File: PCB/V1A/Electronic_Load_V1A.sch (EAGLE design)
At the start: 64 parts, among them J1 +, J2 -, J3 +, J4 -, Q1 IXTK102N65X2, Q2 IXTK102N65X2, Q3 IRF540, Q4 IRF540, Q5 IRF540, Q6 IRF540, U1 LTC1865-MSOP, U2 LTC1865-MSOP, U3 AD420, U4 AD420

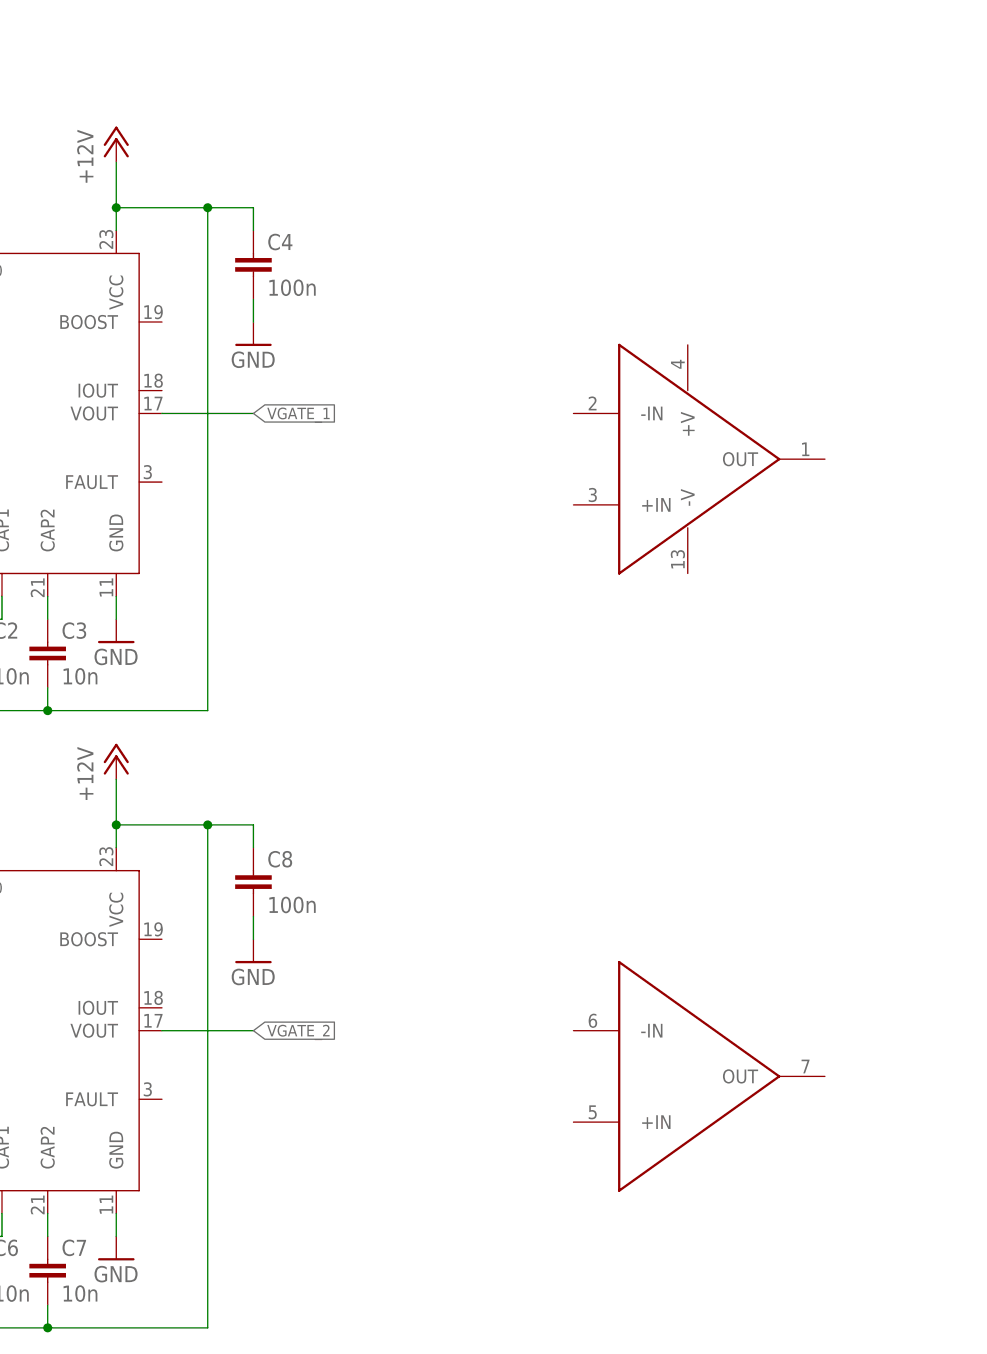
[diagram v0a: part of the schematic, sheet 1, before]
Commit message: Added buffer amplifiers
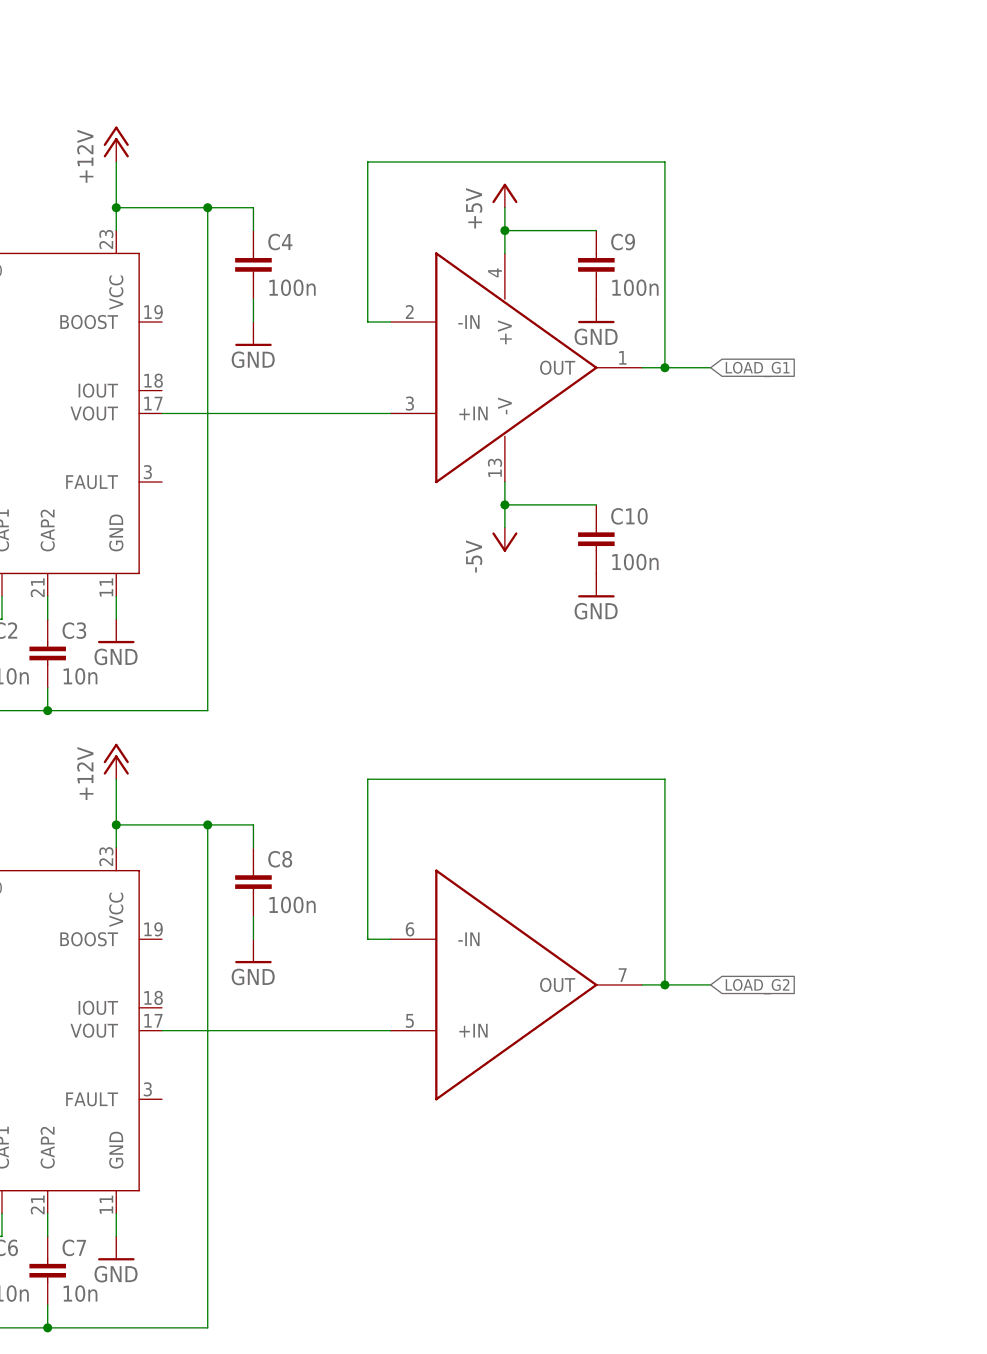
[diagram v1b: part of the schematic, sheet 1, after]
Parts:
- added C10, C9: 100n, rcl:C-EUC0805
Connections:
- net +5V: now also C9.1, U$2G1.+V
- net -5V: now also C10.1, U$2G1.-V
- net GND: now also C10.2, C9.2
- net LOAD_G1: now also U$2G1.-IN, U$2G1.OUT
- net LOAD_G2: now also U$2G2.-IN, U$2G2.OUT
- net VGATE_1: now also U$2G1.+IN
- net VGATE_2: now also U$2G2.+IN
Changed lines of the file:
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@@
 <?xml version="1.0" encoding="utf-8"?>
 <!DOCTYPE eagle SYSTEM "eagle.dtd">
-<eagle version="9.0.0">
+<eagle version="9.0.1">
 <drawing>
 <settings>
@@
 <part name="GND17" library="supply1" library_urn="urn:adsk.eagle:library:371" deviceset="GND" device=""/>
 <part name="U$2" library="SparkFun-Retired" deviceset="LT1014" device=""/>
+<part name="P+12" library="supply1" library_urn="urn:adsk.eagle:library:371" deviceset="+5V" device=""/>
+<part name="P-3" library="supply1" library_urn="urn:adsk.eagle:library:371" deviceset="-5V" device=""/>
+<part name="C9" library="rcl" library_urn="urn:adsk.eagle:library:334" deviceset="C-EU" device="C0805" package3d_urn="urn:adsk.eagle:package:23617/2" value="100n"/>
+<part name="C10" library="rcl" library_urn="urn:adsk.eagle:library:334" deviceset="C-EU" device="C0805" package3d_urn="urn:adsk.eagle:package:23617/2" value="100n"/>
+<part name="GND18" library="supply1" library_urn="urn:adsk.eagle:library:371" deviceset="GND" device=""/>
+<part name="GND19" library="supply1" library_urn="urn:adsk.eagle:library:371" deviceset="GND" device=""/>
 </parts>
 <sheets>
@@
 <instance part="C8" gate="G$1" x="104.14" y="147.32"/>
 <instance part="GND17" gate="1" x="104.14" y="137.16"/>
-<instance part="U$2" gate="G1" x="149.86" y="193.04"/>
-<instance part="U$2" gate="G2" x="149.86" y="124.46"/>
+<instance part="U$2" gate="G1" x="129.54" y="203.2"/>
+<instance part="U$2" gate="G2" x="129.54" y="134.62"/>
 <instance part="U$2" gate="G3" x="-88.9" y="231.14"/>
 <instance part="U$2" gate="G4" x="-91.44" y="180.34"/>
+<instance part="P+12" gate="1" x="132.08" y="223.52"/>
+<instance part="P-3" gate="1" x="132.08" y="182.88"/>
+<instance part="C9" gate="G$1" x="142.24" y="215.9"/>
+<instance part="C10" gate="G$1" x="142.24" y="185.42"/>
+<instance part="GND18" gate="1" x="142.24" y="208.28"/>
+<instance part="GND19" gate="1" x="142.24" y="177.8"/>
 </instances>
 <busses>
@@
 <wire x1="104.14" y1="142.24" x2="104.14" y2="139.7" width="0.1524" layer="91"/>
 </segment>
+<segment>
+<pinref part="C9" gate="G$1" pin="2"/>
+<pinref part="GND18" gate="1" pin="GND"/>
+</segment>
+<segment>
+<pinref part="C10" gate="G$1" pin="2"/>
+<pinref part="GND19" gate="1" pin="GND"/>
+</segment>
 </net>
 <net name="N$1" class="0">
@@
 <label x="198.12" y="114.3" size="1.27" layer="95" font="vector" ratio="12" rot="R180" xref="yes"/>
 <pinref part="R1" gate="G$1" pin="1"/>
+</segment>
+<segment>
+<pinref part="U$2" gate="G1" pin="-IN"/>
+<wire x1="119.38" y1="208.28" x2="116.84" y2="208.28" width="0.1524" layer="91"/>
+<wire x1="116.84" y1="208.28" x2="116.84" y2="226.06" width="0.1524" layer="91"/>
+<wire x1="116.84" y1="226.06" x2="149.86" y2="226.06" width="0.1524" layer="91"/>
+<wire x1="149.86" y1="226.06" x2="149.86" y2="203.2" width="0.1524" layer="91"/>
+<pinref part="U$2" gate="G1" pin="OUT"/>
+<wire x1="149.86" y1="203.2" x2="147.32" y2="203.2" width="0.1524" layer="91"/>
+<wire x1="149.86" y1="203.2" x2="154.94" y2="203.2" width="0.1524" layer="91"/>
+<junction x="149.86" y="203.2"/>
+<label x="154.94" y="203.2" size="1.27" layer="95" font="vector" ratio="12" xref="yes"/>
 </segment>
 </net>
@@
 <wire x1="261.62" y1="114.3" x2="256.54" y2="114.3" width="0.1524" layer="91"/>
 <label x="256.54" y="114.3" size="1.27" layer="95" font="vector" ratio="12" rot="R180" xref="yes"/>
+</segment>
+<segment>
+<pinref part="U$2" gate="G2" pin="-IN"/>
+<wire x1="119.38" y1="139.7" x2="116.84" y2="139.7" width="0.1524" layer="91"/>
+<wire x1="116.84" y1="139.7" x2="116.84" y2="157.48" width="0.1524" layer="91"/>
+<wire x1="116.84" y1="157.48" x2="149.86" y2="157.48" width="0.1524" layer="91"/>
+<wire x1="149.86" y1="157.48" x2="149.86" y2="134.62" width="0.1524" layer="91"/>
+<pinref part="U$2" gate="G2" pin="OUT"/>
+<wire x1="149.86" y1="134.62" x2="147.32" y2="134.62" width="0.1524" layer="91"/>
+<wire x1="149.86" y1="134.62" x2="154.94" y2="134.62" width="0.1524" layer="91"/>
+<junction x="149.86" y="134.62"/>
+<label x="154.94" y="134.62" size="1.27" layer="95" font="vector" ratio="12" xref="yes"/>
 </segment>
 </net>
@@
 <pinref part="P+11" gate="1" pin="+5V"/>
 </segment>
+<segment>
+<pinref part="U$2" gate="G1" pin="+V"/>
+<pinref part="P+12" gate="1" pin="+5V"/>
+<wire x1="132.08" y1="220.98" x2="132.08" y2="218.44" width="0.1524" layer="91"/>
+<pinref part="C9" gate="G$1" pin="1"/>
+<wire x1="132.08" y1="218.44" x2="132.08" y2="215.9" width="0.1524" layer="91"/>
+<wire x1="132.08" y1="218.44" x2="142.24" y2="218.44" width="0.1524" layer="91"/>
+<junction x="132.08" y="218.44"/>
+</segment>
 </net>
 <net name="VGATE_1" class="0">
 <segment>
 <pinref part="U3" gate="G$1" pin="VOUT"/>
-<wire x1="93.98" y1="198.12" x2="104.14" y2="198.12" width="0.1524" layer="91"/>
-<label x="104.14" y="198.12" size="1.27" layer="95" font="vector" ratio="12" xref="yes"/>
+<pinref part="U$2" gate="G1" pin="+IN"/>
+<wire x1="119.38" y1="198.12" x2="93.98" y2="198.12" width="0.1524" layer="91"/>
 </segment>
 </net>
@@
 <segment>
 <pinref part="U4" gate="G$1" pin="VOUT"/>
-<wire x1="93.98" y1="129.54" x2="104.14" y2="129.54" width="0.1524" layer="91"/>
-<label x="104.14" y="129.54" size="1.27" layer="95" font="vector" ratio="12" xref="yes"/>
-</segment>
-</net>
+<pinref part="U$2" gate="G2" pin="+IN"/>
+<wire x1="119.38" y1="129.54" x2="93.98" y2="129.54" width="0.1524" layer="91"/>
+</segment>
+</net>
+<net name="-5V" class="0">
+<segment>
+<pinref part="U$2" gate="G1" pin="-V"/>
+<pinref part="P-3" gate="1" pin="-5V"/>
+<wire x1="132.08" y1="185.42" x2="132.08" y2="187.96" width="0.1524" layer="91"/>
+<pinref part="C10" gate="G$1" pin="1"/>
+<wire x1="132.08" y1="187.96" x2="132.08" y2="190.5" width="0.1524" layer="91"/>
+<wire x1="132.08" y1="187.96" x2="142.24" y2="187.96" width="0.1524" layer="91"/>
+<junction x="132.08" y="187.96"/>
+</segment>
+</net>

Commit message: Updated DAC buffer amps & datasheets
Changed the positive supply of DAC buffer op amps from +5V to +12V, added input offset trimming and set their gain to 2 (1.98). This was done in order to achieve maximum current at low voltages by increasing the maximum gate voltage, and to cailbrate the op amps.
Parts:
- removed C1, C10, C4, C5, C8, C9: 100n, rcl:C-EUC0805
- removed C2, C3, C6, C7: 10n, rcl:C-EUC0805
- removed J1, J3: +, SparkFun-Connectors:BANANA_CONN
- removed J2, J4: -, SparkFun-Connectors:BANANA_CONN
- removed Q1, Q2: IXTK102N65X2, transistors:IXTK102N65X2
- removed Q3, Q4, Q5, Q6: IRF540, transistor-fet:IRF540
- removed R1, R2, R3, R4, R5, R8, R9: 100R, rcl:R-EU_M5923
- removed R10, R6: 2R, rcl:R-EU_M5923
- removed R11, R7: 0R002, rcl:R-EU_M5923
- removed S1: (no value), switch:320-938
- removed U$2: LT1014, SparkFun-Retired:LT1014
- removed U3, U4: AD420, adc_dac:AD420
- added C101, C102, C107, C108, C109, C110: 100n, rcl:C-EUC0805
- added C103, C104, C105, C106: 10n, rcl:C-EUC0805
- added J101, J103: +, SparkFun-Connectors:BANANA_CONN
- added J102, J104: -, SparkFun-Connectors:BANANA_CONN
- added Q101, Q102, Q103, Q105, Q106, Q107: SIRC10DP, transistors:SIRC10DP
- added Q104, Q108: IXTK102N65X2, transistors:IXTK102N65X2
- added R101, R102: 20k, rcl:R-TRIMM4G/J
- added R103, R104: 200k, rcl:R-EU_M5923
- added R105, R106, R111, R112, R113, R114, R115, R118, R119, R120, R121: 100R, rcl:R-EU_M5923
- added R107, R108, R109, R110: 5k, rcl:R-EU_M5923
- added R116, R122: 2R, rcl:R-EU_M5923
- added R117, R123: 0R002, rcl:R-EU_M5923
- added S101: (no value), switch:320-938
- added U101, U102: AD420, adc_dac:AD420
- added U103: LT1014, SparkFun-Retired:LT1014
- renumbered R12 to R201, R13 to R209, R14 to R202, R15 to R205, R16 to R206, R17 to R210, R18 to R213, R19 to R203, R20 to R211, R21 to R204, R22 to R207, R23 to R208, R24 to R212, R25 to R214, R26 to R215, R27 to R223, R28 to R216, R29 to R219, R30 to R220, R31 to R224, R32 to R227, R33 to R217, R34 to R225, R35 to R218, R36 to R221, R37 to R222, R38 to R226, R39 to R228, U$1 to U201, U1 to U202, U2 to U203
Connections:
- new net N$28: R107.2, R109.1, U103G1.-IN
- new net N$29: R108.2, R110.1, U103G2.-IN
- new net N$30: Q101.G, R112.2
- new net N$31: Q105.G, R118.2
- new net N$32: R103.2, R105.2, R107.1
- new net N$33: R101.S, R103.1
- new net N$34: R102.S, R104.1
- new net N$35: R104.2, R106.2, R108.1
- net +12V: now also C103.2, C104.2, C105.2, C106.2, C107.1, C108.1, C109.1, U101.VCC, U102.VCC, U103G1.+V; no longer C2.2, C3.2, C4.1, C6.2, C7.2, C8.1, U3.VCC, U4.VCC
- net +5V: now also C101.1, C102.1, R101.E, R102.E, U101.VLL, U102.VLL; no longer C1.1, C5.1, C9.1, U$2G1.+V, U3.VLL, U4.VLL
- net -5V: now also C110.1, R101.A, R102.A, U103G1.-V; no longer C10.1, U$2G1.-V
- net BYP_G: now also R111.1; no longer R3.1
- net CSENSE_H1: now also Q101.S, Q102.S, Q103.S, R116.1, R117.2; no longer Q3.S, Q4.S, R6.1, R7.2
- net CSENSE_H2: now also Q105.S, Q106.S, Q107.S, R122.1, R123.2; no longer Q5.S, Q6.S, R10.1, R11.2
- net CSENSE_L1: now also Q101.D, Q102.D, Q103.D, Q104.S, R116.2; no longer Q1.S, Q3.D, Q4.D, R6.2
- net CSENSE_L2: now also Q105.D, Q106.D, Q107.D, Q108.S, R122.2; no longer Q2.S, Q5.D, Q6.D, R10.2
- net DUT_+: now also J103.1, Q104.D, Q108.D, S1011.S; no longer J1.1, Q1.D, Q2.D, S11.S
- net GND: now also C101.2, C102.2, C107.2, C108.2, C109.2, C110.2, J104.1, R105.1, R106.1, R117.1, R123.1, S101B.S, U101.GND, U101.RS1, U101.RS2, U102.GND, U102.RS1, U102.RS2; no longer C1.2, C10.2, C4.2, C5.2, C8.2, C9.2, J2.1, R11.1, R7.1, S1B.S, U3.GND, U3.RS1, U3.RS2, U4.GND, U4.RS1, U4.RS2
- net LOAD_G1: now also R109.2, R113.1, U103G1.OUT; no longer R1.1, U$2G1.-IN, U$2G1.OUT
- net LOAD_G2: now also R110.2, R119.1, U103G2.OUT; no longer R2.1, U$2G2.-IN, U$2G2.OUT
- net N$1: now also Q104.G, R113.2; no longer Q1.G, R1.2
- net N$10: now also Q102.G, R114.2; no longer Q3.G, R4.2
- net N$13: now also Q107.G, R121.2; no longer Q6.G, R9.2
- net N$14: now also Q106.G, R120.2; no longer Q5.G, R8.2
- net N$2: now also Q108.G, R119.2; no longer Q2.G, R2.2
- net N$24: now also C106.1, U102.CAP2; no longer C7.1, U4.CAP2
- net N$25: now also C103.1, U101.CAP1; no longer C2.1, U3.CAP1
- net N$26: now also C104.1, U102.CAP1; no longer C6.1, U4.CAP1
- net N$27: now also C105.1, U101.CAP2; no longer C3.1, U3.CAP2
- net N$6: now also R111.2, R112.1, R114.1, R115.1, R118.1, R120.1, R121.1; no longer R3.2, R4.1, R5.1, R8.1, R9.1
- net N$9: now also Q103.G, R115.2; no longer Q4.G, R5.2
- net REM_VSENSE+: now also J101.1, S1011.O; no longer J3.1, S11.O
- net REM_VSENSE-: now also J102.1, S101B.O; no longer J4.1, S1B.O
- net VGATE_1: now also U101.VOUT, U103G1.+IN; no longer U$2G1.+IN, U3.VOUT
- net VGATE_2: now also U102.VOUT, U103G2.+IN; no longer U$2G2.+IN, U4.VOUT
- net VREF: now also U101.REF_IN, U101.REF_OUT, U102.REF_IN; no longer U3.REF_IN, U3.REF_OUT, U4.REF_IN
- net VSENSE+: now also S1011.P; no longer S11.P
- net VSENSE-: now also S101B.P; no longer S1B.P

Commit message: Added MOSFET models, updated info
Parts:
- added HS1, HS2: HEATSINK-LGA115X, mechanical:HEATSINK-LGA115X
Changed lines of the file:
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@@
 <part name="P+106" library="supply1" library_urn="urn:adsk.eagle:library:371" deviceset="+5V" device=""/>
 <part name="GND109" library="supply1" library_urn="urn:adsk.eagle:library:371" deviceset="GND" device=""/>
+<part name="HS1" library="mechanical" deviceset="HEATSINK-LGA115X" device=""/>
+<part name="HS2" library="mechanical" deviceset="HEATSINK-LGA115X" device=""/>
 </parts>
 <sheets>
@@
 <instance part="P+106" gate="1" x="99.06" y="175.26"/>
 <instance part="GND109" gate="1" x="124.46" y="134.62"/>
+<instance part="HS1" gate="G$1" x="248.92" y="139.7"/>
+<instance part="HS2" gate="G$1" x="330.2" y="139.7"/>
 </instances>
 <busses>

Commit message: Added voltage regulators
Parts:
- added C301, C310, C311: 100u, rcl:CPOL-EU085CS-1AR
- added C302: 100n, rcl:C-EUC0805
- added C303, C315: 1u, rcl:CPOL-EU085CS-1AR
- added C304, C306: 10n, rcl:C-EUC0805
- added C305: 10u, rcl:CPOL-EU085CS-1AR
- added C307, C312: 0.33u, rcl:C-EUC0805
- added C308, C314: 0.1u, rcl:C-EUC0805
- added C309: 22u, rcl:CPOL-EU085CS-1AR
- added C313: 2u2, rcl:CPOL-EU085CS-1AR
- added D301, D302: 1N5817-B, diode:1N5817-B
- added D303, D304: 1N4004, diode:1N4004
- added IC301: MAX743CPE, maxim:MAX743CPE
- added IC302, IC303: 7805T, linear:7805T
- added IC304: (no value), linear:7905T
- added J301: (no value), con-jack:JACK-PLUG0
- added L301, L302: 100u, rcl:L-EU0204/5
- added R1, R10, R2, R3, R4, R5, R6, R7, R8, R9: 1M, rcl:R-EU_R2512
- added R11: (no value), rcl:R-EU_R2512
- added R12, R13, R14, R15: 5k, rcl:R-EU_M5923
- added U1: LT1014, SparkFun-Retired:LT1014
- renumbered HS1 to HS101, HS2 to HS102
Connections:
- new net +15V: C109.1, C310.+, C312.1, D301.C, IC301.FB+, IC303.VI, U103G1.+V, U201G1.+V
- new net +5V/1: C314.1, D303.C, IC303.VO, R101.E, R102.E, R213.A, R214.A, R227.A, R228.A
- new net -15V: C110.1, C311.-, C313.-, D302.A, IC301.FB-, IC304.VI, U103G1.-V, U201G1.-V
- new net N$36: D301.A, IC301.LX+, L302.2
- new net N$37: C306.1, IC301.CC-
- new net N$38: C303.+, IC301.SS
- new net N$39: D302.C, IC301.LX-, L301.1
- new net N$40: C304.2, IC301.CC+
- new net N$41: R1.1, R2.2
- new net N$42: R2.1, R3.2
- new net N$43: R3.1, R4.2
- new net N$44: C307.2, C308.2, IC302.GND
- new net N$45: R4.1, R5.1
- new net N$46: R5.2, R6.1
- new net N$47: R6.2, R7.1
- new net N$48: R7.2, R8.1
- new net N$49: R8.2, R9.2
- new net N$50: R10.2, R9.1
- new net N$51: R10.1, R11.2
- new net N$53: R1.2
- net +12V: now also C301.+, C307.1, IC302.VI, J301.3; no longer C109.1, U103G1.+V
- net +5V: now also C302.2, C308.1, C309.+, IC301.AV+, IC301.V+, IC301.V+@1, IC301.V+@2, IC301.V+@3, IC302.VO, L302.1; no longer R101.E, R102.E, R213.A, R214.A, R227.A, R228.A, U201G1.+V
- net -5V: now also C315.-, D304.A, IC304.VO; no longer C110.1, U103G1.-V, U201G1.-V
- net GND: now also C301.-, C302.1, C303.-, C304.1, C305.-, C306.2, C309.-, C310.-, C311.+, C312.2, C313.+, C314.2, C315.+, D303.A, D304.C, IC301.12/15, IC301.AGND, IC301.GND, IC303.GND, IC304.GND, J301.1, J301.2, L301.2, R11.1
- net VREF: now also C305.+, IC301.VREF
